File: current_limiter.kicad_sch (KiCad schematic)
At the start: 39 parts, among them J1 VIN, J2 VOUT, J3 CS-, J4 CS+, Q1 BSC040N10NS5, Q2 BC849, Q3 BC858, U1 TLV1805QDBVRQ1, U2 INA181A2IDBVR, U3 OPA991IDCKR

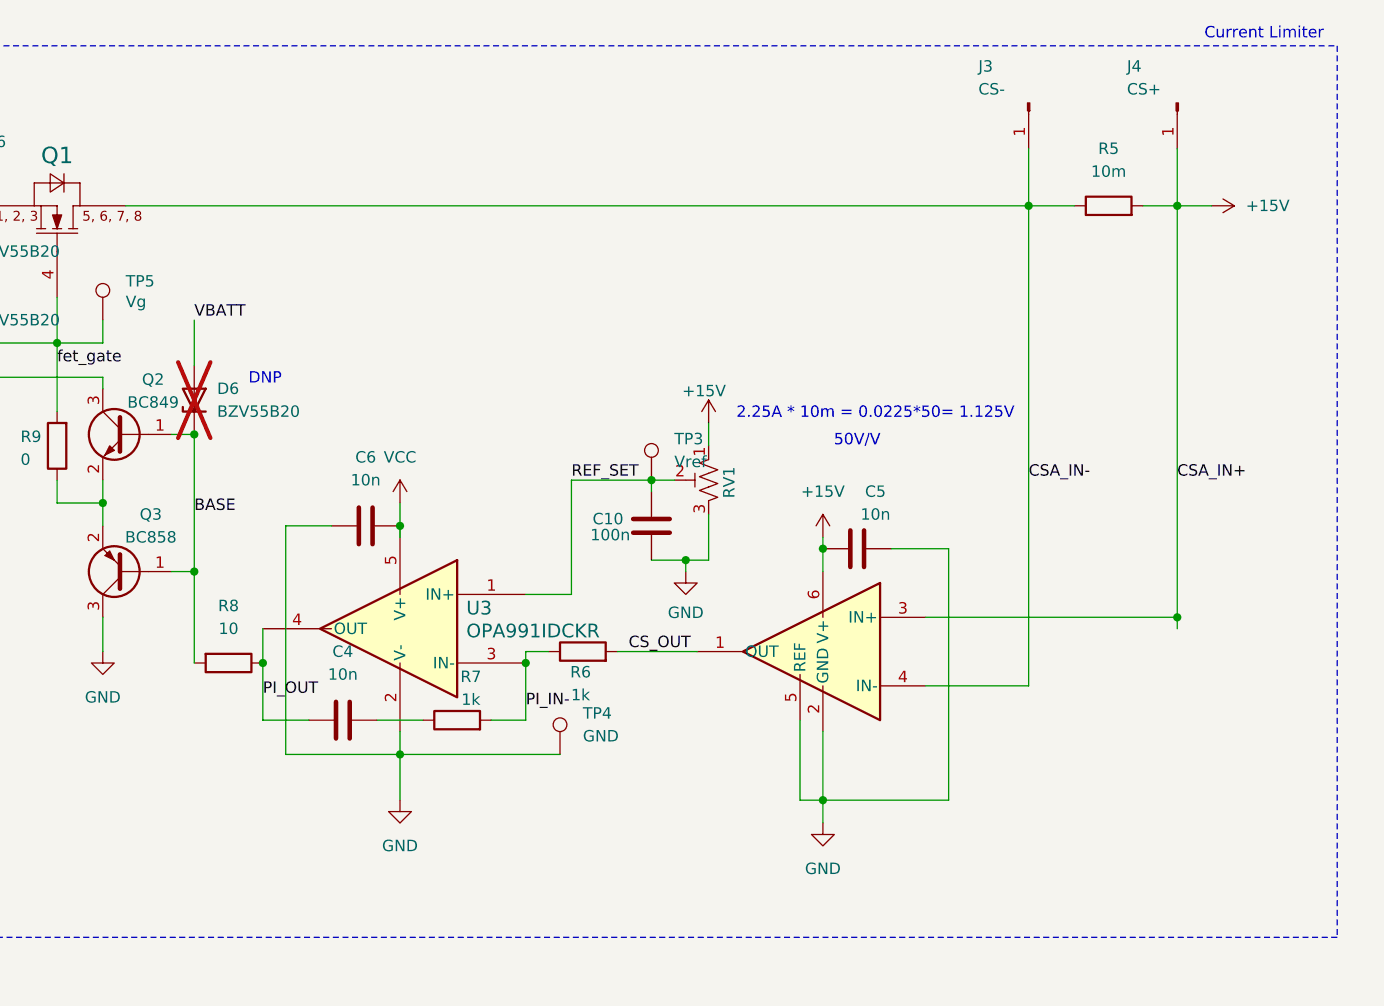
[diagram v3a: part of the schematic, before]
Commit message: version 3: updated to 4-layer board, added shunts + various current-limiting resistors, changed reference to have maximum value of 5A
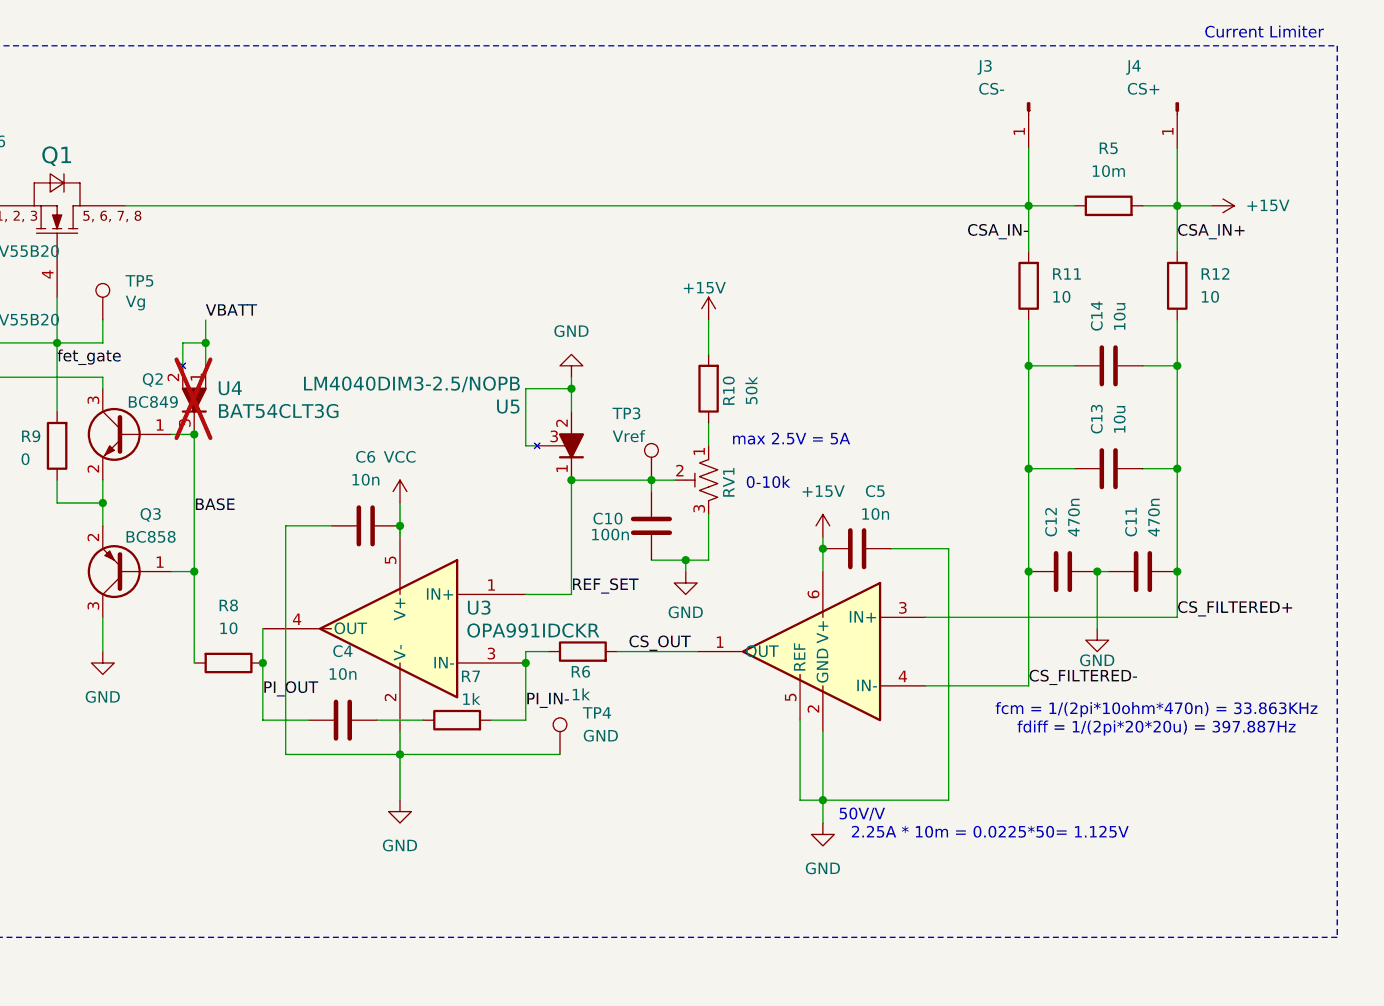
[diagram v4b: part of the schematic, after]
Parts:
- removed D6: BZV55B20, Diode_SMD:D_MiniMELF, symbol Diode:BZV55B20
- added C11, C12: 470n, Capacitor_SMD:C_0402_1005Metric, symbol Device:C
- added C13, C14: 10u, Capacitor_SMD:C_0402_1005Metric, symbol Device:C
- added R10: 50k, Capacitor_SMD:C_0805_2012Metric, symbol Device:R
- added R11, R12: 10, Resistor_SMD:R_0402_1005Metric, symbol Device:R
- added U4: BAT54CLT3G, Current_Limiter_Stuff:SOT-23-3_1P4X3P040_ONS, symbol Current-limiter-stuff:BAT54CLT3G
- added U5: LM4040DIM3-2.5/NOPB, Current_Limiter_Stuff:DBZ3, symbol Current-limiter-stuff:LM4040DIM3-2.5_NOPB
- C2, C3, C8, C9: footprint Capacitor_SMD:C_1206_3216Metric -> Capacitor_SMD:C_0805_2012Metric
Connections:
- net +15V: now also R10.2, R12.2; no longer RV1.1, U2.3 (IN+)
- net BASE: now also U4.3
- net CSA_IN-: now also R11.2; no longer U2.4 (IN-)
- net GND: now also C11.2, C12.1, U5.2, U5.3
- net REF_SET: now also U5.1
- net VBATT: now also U4.1, U4.2
- new net: R10.1, RV1.1
- new net CS_FILTERED+: C11.1, C13.1, C14.1, R12.1, U2.3 (IN+)
- new net CS_FILTERED-: C12.2, C13.2, C14.2, R11.1, U2.4 (IN-)
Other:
- note added: "0-10k"
- note added: "fcm = 1/(2pi*10ohm*470n) = 33.863KHz fdiff = 1/(2pi*20*20u) = 397.887Hz"
- note added: "max 2.5V = 5A"
- note removed: "DNP"

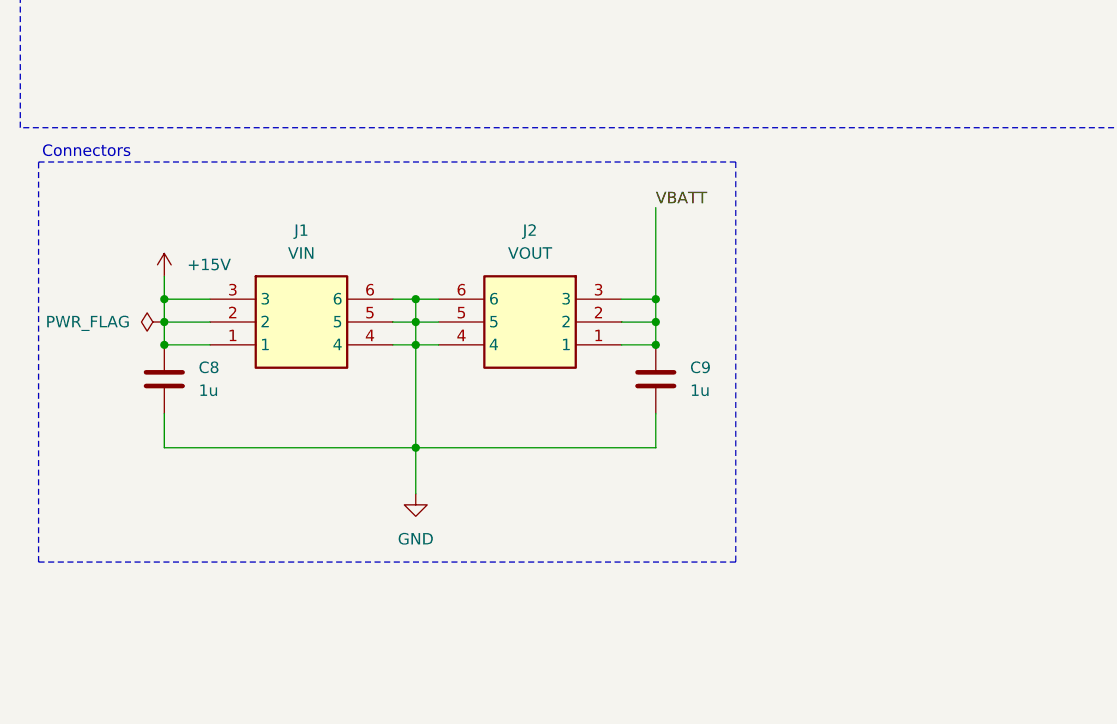
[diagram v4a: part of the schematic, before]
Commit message: minor revisions, changed molex to banana plug and readjusted zones
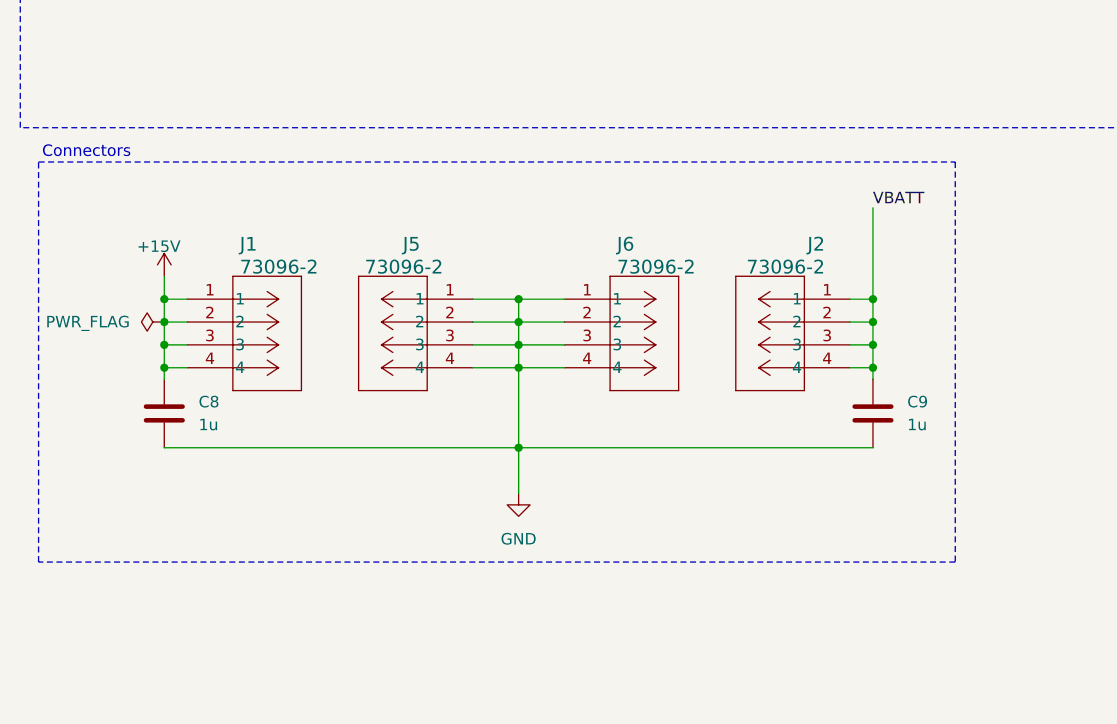
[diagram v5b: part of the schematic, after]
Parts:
- removed J1: VIN, Current_Limiter_Stuff:4304506YY_6, symbol Current_Limiter_Stuff:430450627 Molex
- removed J2: VOUT, Current_Limiter_Stuff:4304506YY_6, symbol Current_Limiter_Stuff:430450627 Molex
- added J1, J2, J5, J6: 73096-2, CONN_73096-2_POM, symbol Current-limiter-stuff:73096-2
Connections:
- net +15V: now also J1.1, J1.2, J1.3, J1.4
- net GND: now also J5.1, J5.2, J5.3, J5.4, J6.1, J6.2, J6.3, J6.4
- net VBATT: now also J2.1, J2.2, J2.3, J2.4
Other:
- moved on the sheet: C8, C9

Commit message: minor revisions: added mounting holes, changed one track to back signal layer
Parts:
- added H1, H2, H3, H4: MountingHole, MountingHole:MountingHole_4.3mm_M4, symbol Mechanical:MountingHole
- J1, J2, J5, J6: footprint CONN_73096-2_POM -> Current_Limiter_Stuff:CONN_73096-2_POM
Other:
- note added: "Mounting Holes"

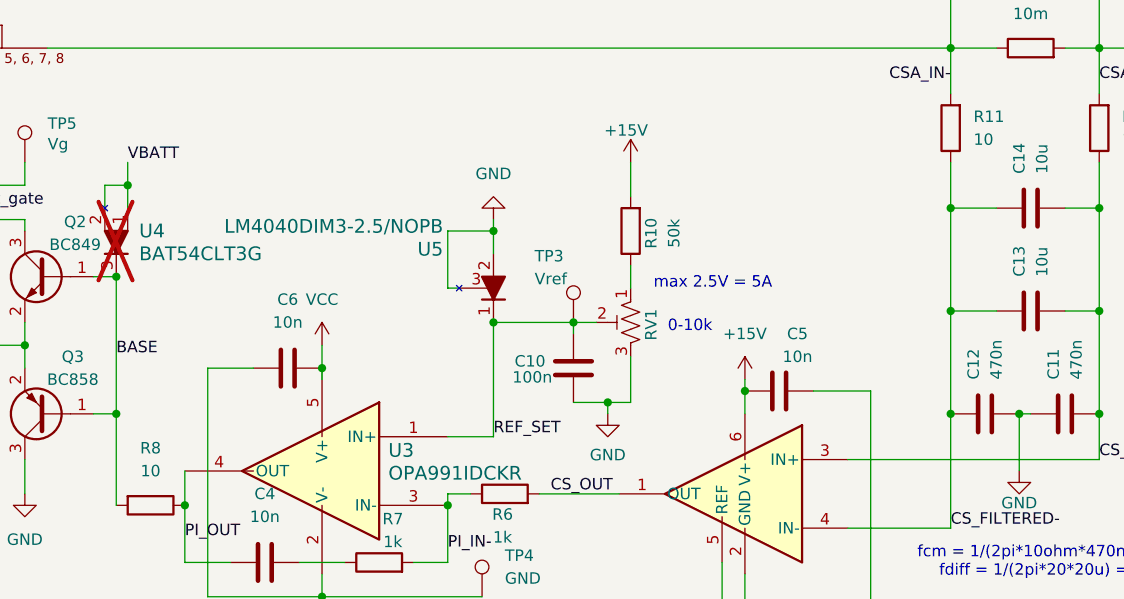
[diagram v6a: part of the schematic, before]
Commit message: proper shunt setup, properly calculated resistance values necessary for shunt diode to operate safely
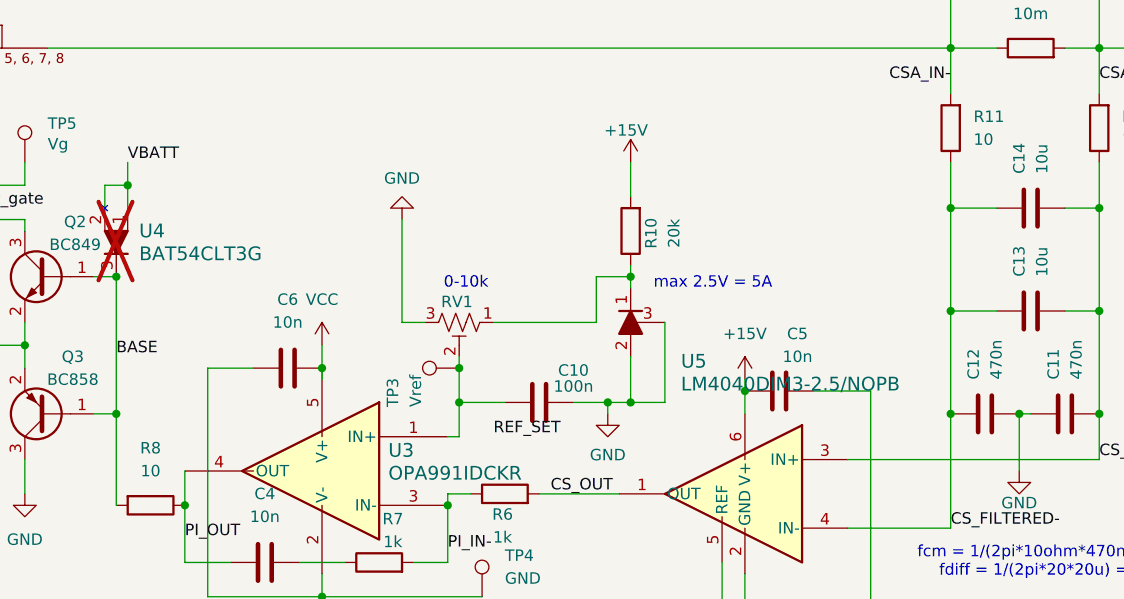
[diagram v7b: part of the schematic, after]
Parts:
- R10: value 50k -> 20k
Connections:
- net REF_SET: no longer C10.2, RV1.2, TP3.1, U3.1 (IN+), U5.1
- net at R10.1, RV1.1: now also U5.1
- new net: C10.2, RV1.2, TP3.1, U3.1 (IN+)
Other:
- moved on the sheet: C10, RV1, TP3

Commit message: minor update: changed resistor value from 20k to 22k for E12 value
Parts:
- R10: value 20k -> 22k
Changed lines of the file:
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@@
 			)
 		)
-		(property "Value" "20k"
+		(property "Value" "22k"
 			(at 216.916 56.134 90)
 			(show_name no)
